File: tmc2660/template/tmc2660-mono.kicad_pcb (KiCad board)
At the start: 4 copper layers, 25 x 40 mm, 18 parts, among them J100 0R, M100 Mount, M101 Mount, P100 Motor, U100 TMC2660

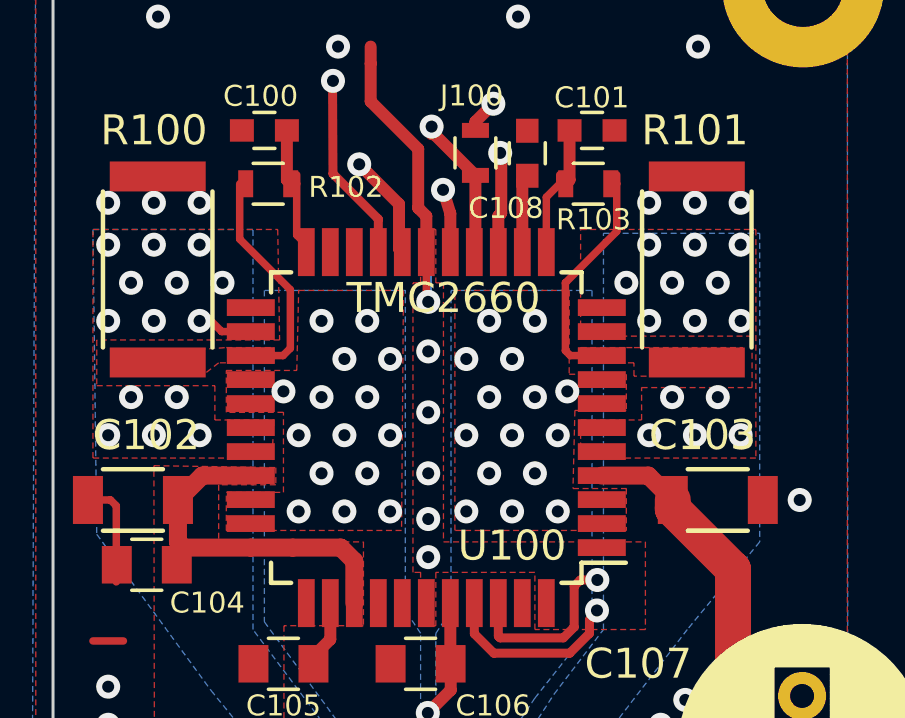
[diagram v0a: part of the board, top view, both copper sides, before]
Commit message: More cooling for input VMOT and output current for bondwire cooling.
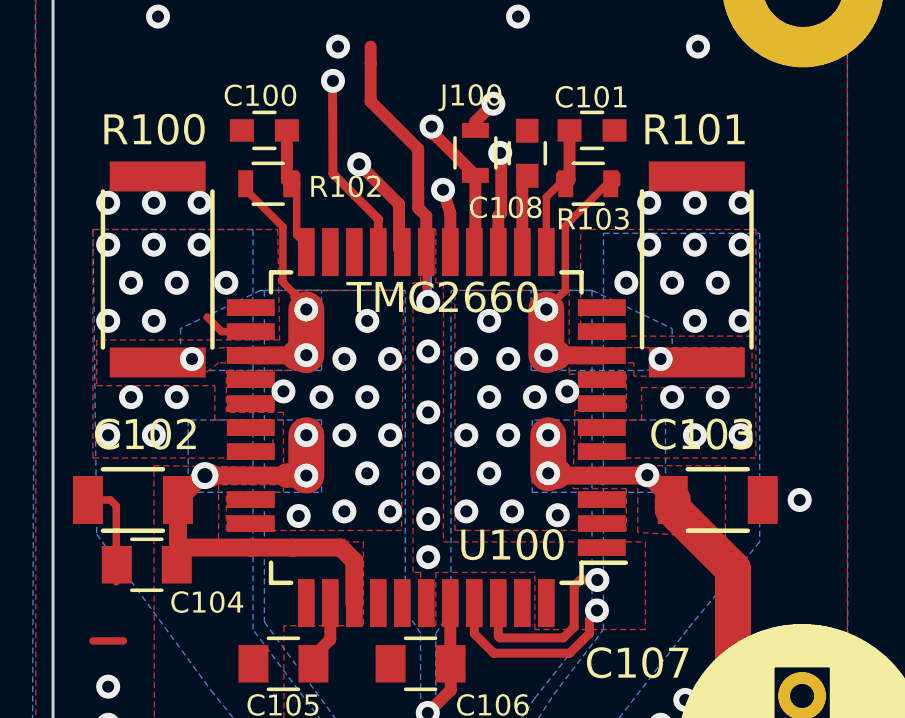
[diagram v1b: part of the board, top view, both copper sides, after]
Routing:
- net VMot: track 26.3 -> 32.8 mm, vias 6 -> 12
- net /TMC2660-100/BRA: track 8.42 -> 9.38 mm, vias 0 -> 3
- net /TMC2660-100/BRB: track 7.60 -> 8.40 mm, vias 0 -> 3
- net /TMC2660-100/B2: vias 14 -> 12
- net /TMC2660-100/B1: vias 15 -> 12
- net /TMC2660-100/A2: vias 14 -> 12
- net /TMC2660-100/A1: vias 15 -> 12
- added copper zone on B.Cu, net /TMC2660-100/BRA
- added copper zone on In1.Cu, net /TMC2660-100/BRA
- added copper zone on In2.Cu, net /TMC2660-100/BRA
- added copper zone on B.Cu, net /TMC2660-100/BRB
- added copper zone on In1.Cu, net /TMC2660-100/BRB
- added copper zone on In2.Cu, net /TMC2660-100/BRB

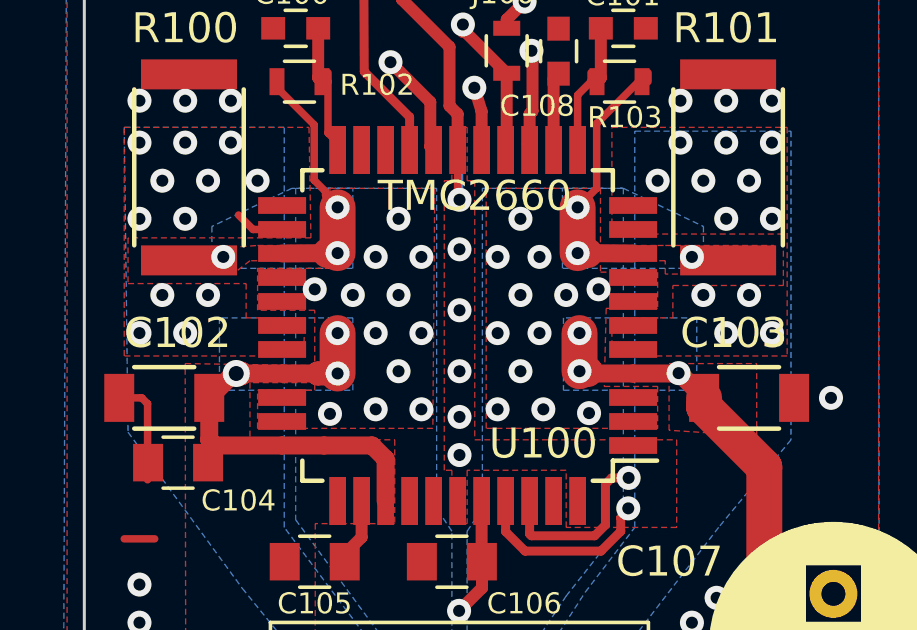
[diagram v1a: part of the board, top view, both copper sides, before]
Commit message: Keep vias out of pads.
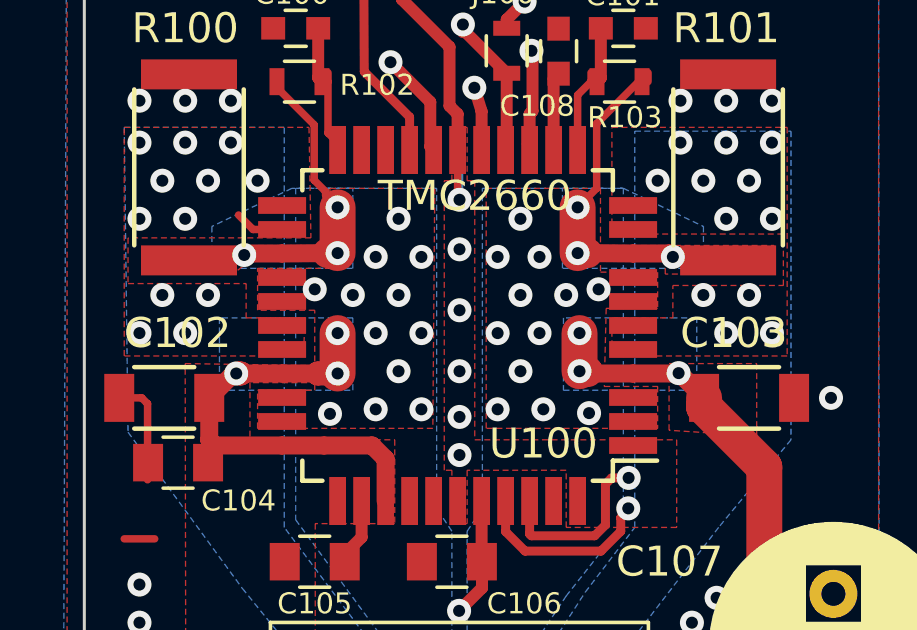
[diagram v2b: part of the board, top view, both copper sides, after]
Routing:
- net /TMC2660-100/BRA: track 9.38 -> 12.6 mm
- net /TMC2660-100/BRB: track 8.40 -> 11.6 mm
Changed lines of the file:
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@@
     (thickness 1.6)
     (drawings 4)
-    (tracks 250)
+    (tracks 258)
     (zones 0)
     (modules 18)
@@
   (segment (start 105.0638 78.8062) (end 105.214298 78.8062) (width 0.8) (layer F.Cu) (net 2))
   (segment (start 105.214298 78.8062) (end 105.214498 78.806) (width 0.8) (layer F.Cu) (net 2))
-  (via (at 105.0638 78.8062) (size 0.9) (drill 0.5) (layers F.Cu B.Cu) (net 2))
+  (via (at 105.0638 78.8062) (size 0.8) (drill 0.4) (layers F.Cu B.Cu) (net 2))
   (via (at 101.838 85.842) (size 0.8) (drill 0.4) (layers F.Cu B.Cu) (net 1))
   (via (at 101.838 87.112) (size 0.8) (drill 0.4) (layers F.Cu B.Cu) (net 1))
@@
   (segment (start 112.492 86.7183) (end 112.506 88.636) (width 0.6) (layer In2.Cu) (net 3))
   (via (at 112.492 86.7183) (size 0.8) (drill 0.4) (layers F.Cu B.Cu) (net 3))
+  (segment (start 119.618 74.92) (end 121.344 74.92) (width 0.6) (layer F.Cu) (net 4))
+  (segment (start 121.344 74.92) (end 121.4595 75.0355) (width 0.6) (layer F.Cu) (net 4))
+  (segment (start 118.2925 74.806) (end 119.504 74.806) (width 0.6) (layer F.Cu) (net 4))
+  (segment (start 119.504 74.806) (end 119.618 74.92) (width 0.6) (layer F.Cu) (net 4))
   (segment (start 117.078 70.475) (end 117.078 72.634) (width 0.25) (layer F.Cu) (net 4))
   (segment (start 117.078 72.634) (end 116.443 73.269) (width 0.25) (layer F.Cu) (net 4))
@@
   (segment (start 116.443 74.793) (end 116.782499 74.793) (width 1) (layer F.Cu) (net 4))
   (segment (start 116.443 73.269) (end 116.443 74.793) (width 1.2) (layer F.Cu) (net 4))
-  (via (at 120.253 74.92) (size 0.8) (drill 0.4) (layers F.Cu B.Cu) (net 4))
+  (via (at 119.618 74.92) (size 0.8) (drill 0.4) (layers F.Cu B.Cu) (net 4))
   (segment (start 118.475 69.078) (end 118.59 69.078) (width 0.25) (layer F.Cu) (net 4))
   (segment (start 117.078 70.475) (end 118.475 69.078) (width 0.25) (layer F.Cu) (net 4))
+  (segment (start 105.3305 74.8565) (end 103.668 74.8565) (width 0.6) (layer F.Cu) (net 5))
+  (segment (start 103.668 74.8565) (end 103.489 75.0355) (width 0.6) (layer F.Cu) (net 5))
+  (segment (start 106.5925 74.806) (end 105.381 74.806) (width 0.6) (layer F.Cu) (net 5))
+  (segment (start 105.381 74.806) (end 105.3305 74.8565) (width 0.6) (layer F.Cu) (net 5))
   (segment (start 108.442 73.269) (end 108.042001 72.869001) (width 0.25) (layer F.Cu) (net 5))
   (segment (start 108.042001 72.869001) (end 108.042001 72.742001) (width 0.25) (layer F.Cu) (net 5))
@@
   (segment (start 108.442 74.793) (end 108.102501 74.793) (width 1) (layer F.Cu) (net 5))
   (segment (start 108.442 74.793) (end 108.442 73.269) (width 1.2) (layer F.Cu) (net 5))
-  (via (at 104.632 74.92) (size 0.8) (drill 0.4) (layers F.Cu B.Cu) (net 5))
+  (via (at 105.3305 74.8565) (size 0.8) (drill 0.4) (layers F.Cu B.Cu) (net 5))
   (segment (start 114.8425 71.356) (end 114.8425 70.156) (width 0.4) (layer F.Cu) (net 6))
   (segment (start 114.939501 68.083801) (end 114.905 68.0493) (width 0.4) (layer F.Cu) (net 6))

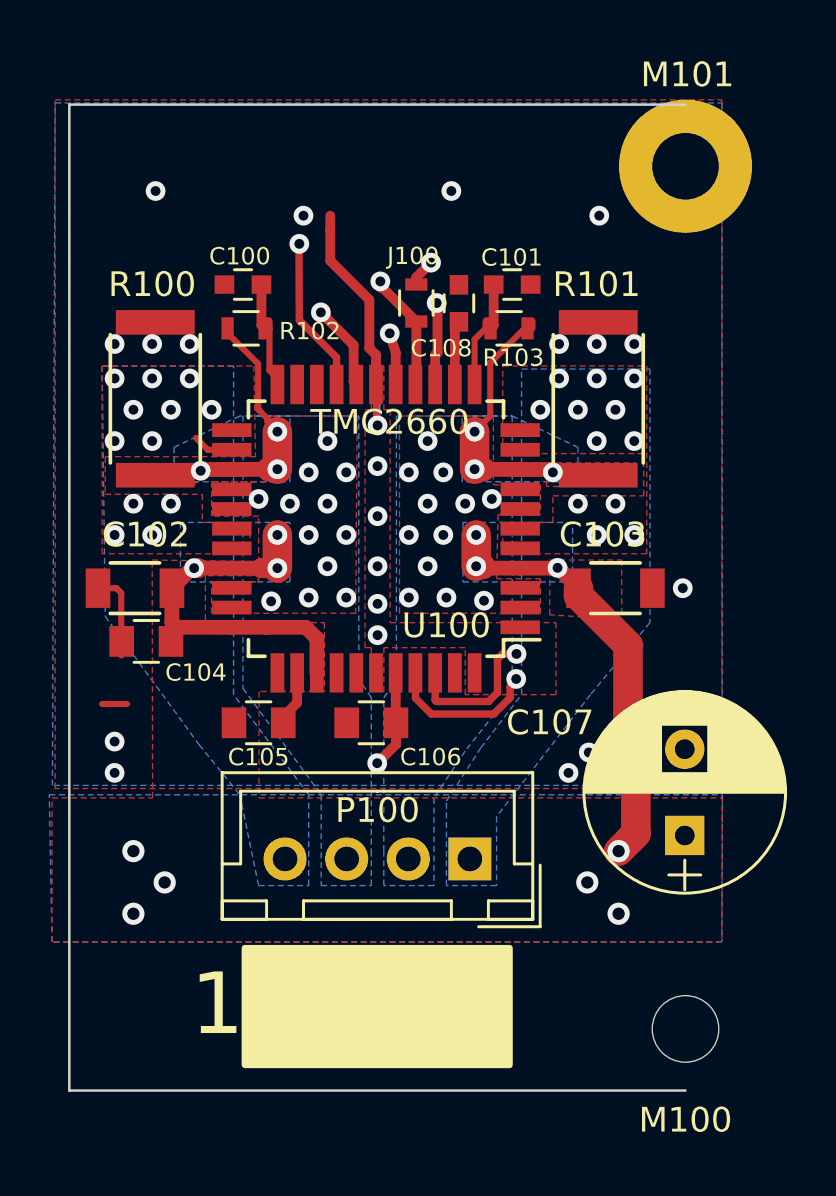
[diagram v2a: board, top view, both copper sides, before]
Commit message: Tweaking vias around vmot pins.
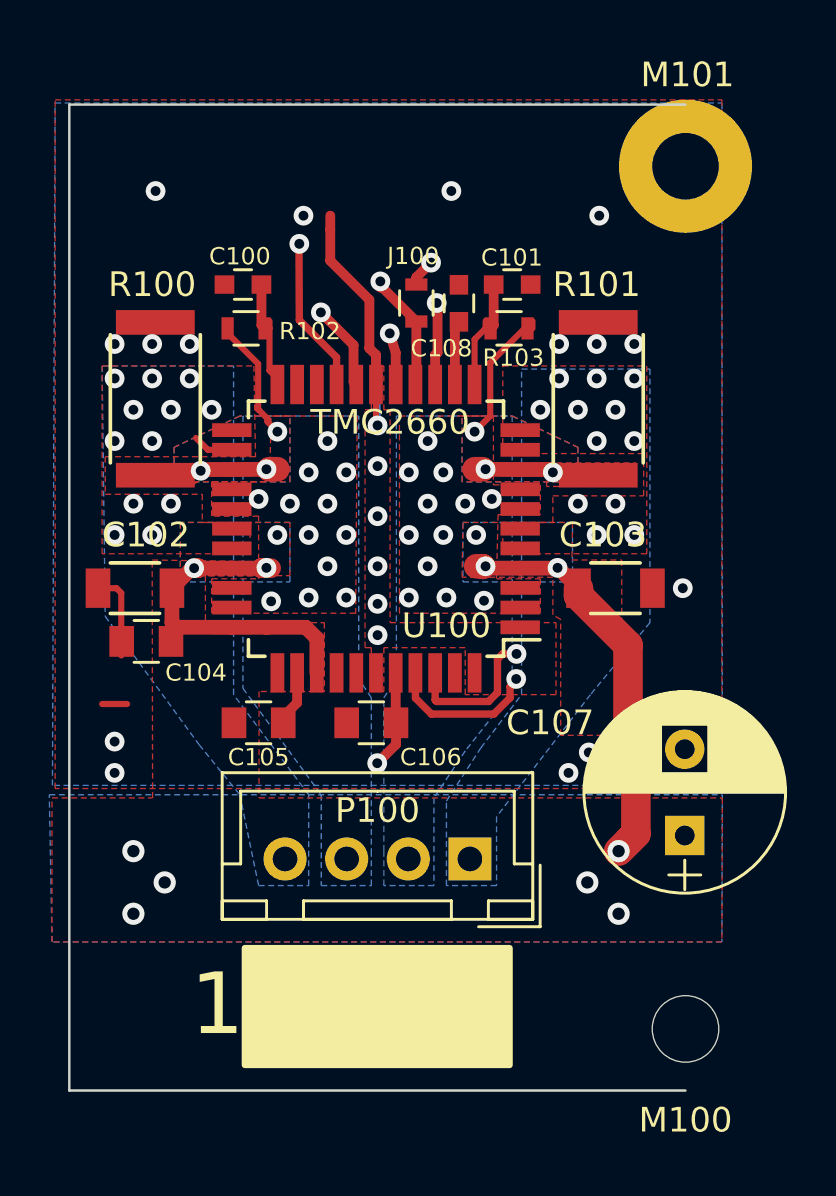
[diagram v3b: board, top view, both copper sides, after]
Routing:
- net VMot: track 32.8 -> 30.2 mm
- net /TMC2660-100/BRB: track 11.6 -> 10.1 mm
- net /TMC2660-100/BRA: track 12.6 -> 11.1 mm
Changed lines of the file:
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@@
     (thickness 1.6)
     (drawings 4)
-    (tracks 258)
+    (tracks 254)
     (zones 0)
     (modules 18)
@@
   )
   (setup
-    (last_trace_width 0.6)
+    (last_trace_width 0.25)
     (user_trace_width 0.2)
     (user_trace_width 0.3)
@@
   (segment (start 116.5065 78.73) (end 116.782499 78.73) (width 1) (layer F.Cu) (net 2))
   (segment (start 116.782499 78.73) (end 116.782499 78.757999) (width 1) (layer F.Cu) (net 2))
-  (segment (start 116.5065 77.46) (end 116.5065 78.73) (width 1.2) (layer F.Cu) (net 2))
   (via (at 119.8085 78.7935) (size 0.8) (drill 0.4) (layers F.Cu B.Cu) (net 2))
-  (segment (start 108.442 78.8062) (end 108.442 77.46) (width 1.2) (layer F.Cu) (net 2))
   (segment (start 105.214498 78.806) (end 106.5925 78.806) (width 0.6) (layer F.Cu) (net 2))
   (segment (start 104.9765 78.806) (end 105.214498 78.806) (width 0.6) (layer F.Cu) (net 2))
@@
   (segment (start 118.2925 74.806) (end 116.782499 74.793) (width 0.6) (layer F.Cu) (net 4))
   (segment (start 116.443 74.793) (end 116.782499 74.793) (width 1) (layer F.Cu) (net 4))
-  (segment (start 116.443 73.269) (end 116.443 74.793) (width 1.2) (layer F.Cu) (net 4))
   (via (at 119.618 74.92) (size 0.8) (drill 0.4) (layers F.Cu B.Cu) (net 4))
   (segment (start 118.475 69.078) (end 118.59 69.078) (width 0.25) (layer F.Cu) (net 4))
@@
   (segment (start 106.5925 74.806) (end 108.102501 74.793) (width 0.6) (layer F.Cu) (net 5))
   (segment (start 108.442 74.793) (end 108.102501 74.793) (width 1) (layer F.Cu) (net 5))
-  (segment (start 108.442 74.793) (end 108.442 73.269) (width 1.2) (layer F.Cu) (net 5))
   (via (at 105.3305 74.8565) (size 0.8) (drill 0.4) (layers F.Cu B.Cu) (net 5))
   (segment (start 114.8425 71.356) (end 114.8425 70.156) (width 0.4) (layer F.Cu) (net 6))
@@
   (via (at 112.506 73.015) (size 0.8) (drill 0.4) (layers F.Cu B.Cu) (net 1))
   (via (at 116.443 73.269) (size 0.8) (drill 0.4) (layers F.Cu B.Cu) (net 4))
-  (via (at 116.443 74.793) (size 0.8) (drill 0.4) (layers F.Cu B.Cu) (net 4))
+  (via (at 116.8875 74.793) (size 0.8) (drill 0.4) (layers F.Cu B.Cu) (net 4))
   (via (at 116.5065 77.46) (size 0.8) (drill 0.4) (layers F.Cu B.Cu) (net 2))
-  (via (at 116.5065 78.73) (size 0.8) (drill 0.4) (layers F.Cu B.Cu) (net 2))
+  (via (at 116.8875 78.73) (size 0.8) (drill 0.4) (layers F.Cu B.Cu) (net 2))
   (via (at 117.1415 75.9995) (size 0.8) (drill 0.4) (layers F.Cu B.Cu) (net 13))
   (via (at 114.538 73.65) (size 0.8) (drill 0.4) (layers F.Cu B.Cu) (net 13))
@@
   (via (at 122.92 77.46) (size 0.8) (drill 0.4) (layers F.Cu B.Cu) (net 14))
   (via (at 121.396 77.46) (size 0.8) (drill 0.4) (layers F.Cu B.Cu) (net 14))
-  (via (at 108.442 78.8062) (size 0.8) (drill 0.4) (layers F.Cu B.Cu) (net 2))
-  (via (at 108.442 74.793) (size 0.8) (drill 0.4) (layers F.Cu B.Cu) (net 5))
+  (via (at 107.9975 78.7935) (size 0.8) (drill 0.4) (layers F.Cu B.Cu) (net 2))
+  (via (at 107.9975 74.793) (size 0.8) (drill 0.4) (layers F.Cu B.Cu) (net 5))
   (via (at 108.442 73.269) (size 0.8) (drill 0.4) (layers F.Cu B.Cu) (net 5))
   (via (at 104.124 72.38) (size 0.8) (drill 0.4) (layers F.Cu B.Cu) (net 15))
@@
   )
   (zone (net 14) (net_name /TMC2660-100/A2) (layer F.Cu) (hatch edge 0.508)
-    (priority 2)
+    (priority 3)
     (connect_pads yes (clearance 0.254))
     (min_thickness 0.254)
@@
     (polygon
       (pts
-        (xy 111.617 80.635) (xy 105.775 80.635) (xy 105.775 79.365) (xy 107.68 79.365) (xy 107.68 76.698)
+        (xy 111.617 80.635) (xy 105.775 80.635) (xy 105.775 79.238) (xy 107.68 79.238) (xy 107.68 76.698)
         (xy 105.775 76.698) (xy 105.775 75.301) (xy 108.1245 75.301) (xy 108.188 72.634) (xy 111.6805 72.634)
       )
@@
   )
   (zone (net 15) (net_name /TMC2660-100/B2) (layer F.Cu) (hatch edge 0.508)
-    (priority 1)
+    (priority 3)
     (connect_pads yes (clearance 0.254))
     (min_thickness 0.254)
@@
     (polygon
       (pts
-        (xy 108.95 72.634) (xy 106.918 72.634) (xy 104.251 73.904) (xy 104.251 75.301) (xy 108.95 75.301)
+        (xy 108.95 72.634) (xy 106.918 72.634) (xy 104.251 73.904) (xy 104.251 75.2375) (xy 108.95 75.2375)
       )
     )
@@
     (polygon
       (pts
-        (xy 108.95 72.634) (xy 106.918 72.634) (xy 104.251 73.904) (xy 104.251 75.301) (xy 108.95 75.301)
+        (xy 108.95 72.634) (xy 106.918 72.634) (xy 104.251 73.904) (xy 104.251 75.2375) (xy 108.95 75.2375)
       )
     )
@@
     (polygon
       (pts
-        (xy 115.937548 72.634) (xy 117.969548 72.634) (xy 120.636548 73.904) (xy 120.636548 75.301) (xy 115.937548 75.301)
+        (xy 115.937548 72.634) (xy 117.969548 72.634) (xy 120.636548 73.904) (xy 120.634 75.2375) (xy 115.935 75.2375)
       )
     )
@@
     (polygon
       (pts
-        (xy 115.937548 72.634) (xy 117.969548 72.634) (xy 120.636548 73.904) (xy 120.636548 75.301) (xy 115.937548 75.301)
+        (xy 115.937548 72.634) (xy 117.969548 72.634) (xy 120.636548 73.904) (xy 120.634 75.2375) (xy 115.935 75.2375)
       )
     )
@@
   )
   (zone (net 2) (net_name VMot) (layer F.Cu) (hatch edge 0.508)
-    (priority 1)
-    (connect_pads yes (clearance 0.3))
-    (min_thickness 0.254)
-    (fill yes (arc_segments 16) (thermal_gap 0.508) (thermal_bridge_width 0.508))
-    (polygon
-      (pts
-        (xy 119.491 78.476) (xy 122.412 78.476) (xy 122.412 80.889) (xy 119.491 80.6985)
-      )
-    )
+    (priority 2)
+    (connect_pads yes (clearance 0.3))
+    (min_thickness 0.254)
+    (fill yes (arc_segments 16) (thermal_gap 0.508) (thermal_bridge_width 0.508))
+    (polygon
+      (pts
+        (xy 120.391246 78.476) (xy 122.412 78.476) (xy 122.412 85.588) (xy 119.9355 85.588) (xy 119.9355 80.889)
+        (xy 119.618 80.6985) (xy 119.618 79.1745) (xy 115.935 79.1745) (xy 115.970782 76.952) (xy 120.415782 76.952)
+      )
+    )
+  )
+  (zone (net 5) (net_name /TMC2660-100/BRB) (layer F.Cu) (hatch edge 0.508)
+    (priority 2)
+    (connect_pads yes (clearance 0.3))
+    (min_thickness 0.254)
+    (fill yes (arc_segments 16) (thermal_gap 0.508) (thermal_bridge_width 0.508))
+    (polygon
+      (pts
+        (xy 108.95 72.634) (xy 106.918 72.634) (xy 104.251 73.904) (xy 104.251 75.301) (xy 108.95 75.301)
+      )
+    )
+  )
+  (zone (net 2) (net_name VMot) (layer F.Cu) (hatch edge 0.508)
+    (priority 2)
+    (connect_pads yes (clearance 0.3))
+    (min_thickness 0.254)
+    (fill yes (arc_segments 16) (thermal_gap 0.508) (thermal_bridge_width 0.508))
+    (polygon
+      (pts
+        (xy 108.95 76.952) (xy 104.505 76.952) (xy 104.505 79.111) (xy 108.95 79.111)
+      )
+    )
+  )
+  (zone (net 4) (net_name /TMC2660-100/BRA) (layer F.Cu) (hatch edge 0.508)
+    (priority 2)
+    (connect_pads yes (clearance 0.3))
+    (min_thickness 0.254)
+    (fill yes (arc_segments 16) (thermal_gap 0.508) (thermal_bridge_width 0.508))
+    (polygon
+      (pts
+        (xy 115.937548 72.634) (xy 117.969548 72.634) (xy 120.636548 73.904) (xy 120.636548 75.301) (xy 115.937548 75.301)
+      )
+    )
